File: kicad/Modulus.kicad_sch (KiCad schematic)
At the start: 230 parts, among them J1 XLR3, J2 USB_C_Receptacle_USB2.0_16P, J3 USB_A, J4 USB_A, J5 XLR3, J6 OLED_128x32, P1 Keyswitch, Q1 Keyswitch, SW1 Push_Button, T1 Keyswitch, U1 RP2040, U3 W25Q128JVS, U4 NCP1117-3.3_SOT223, Y1 12MHz, Y2 12MHz

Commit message: added numpad+macropad
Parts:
- added A1: Raspberry_Pi_Pico_THT, PCM_SL_Development_Boards:raspberry_pi_pico_THT, symbol PCM_SL_Development_Board:Raspberry_Pi_Pico_THT
- added D1, D10, D11, D12, D13, D14, D15, D16, D17, D18, D19, D2, D20, D21, D22, D23, D25, D3, D4, D5, D6, D7, D8, D9: Diode, Diode_SMD:D_SMA, symbol SCOTOKEEBS:Placeholder_Diode
- added D24: D_Generic, symbol PCM_4ms_Diode:D_Generic
- added J10, J9: XLR3, NC3FAAH:NEUTRIK_NC3FAAH, symbol Connector_Audio:XLR3
- added S1, S10, S11, S12, S13, S14, S15, S16, S17, S18, S19, S2, S20, S21, S22, S23, S25, S3, S4, S5, S6, S7, S8, S9: ~, symbol ScottoKeebs_KiCAD:Placeholder_Keyswitch
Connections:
- net GND: now also A1.13 (GND), A1.18 (GND), A1.23 (GND), A1.28 (GND), A1.3 (GND), A1.33 (GND), A1.38 (GND), A1.8 (GND), J9.1
- new net: D16.2 (A), S14.2
- new net: D20.2 (A), S19.2
- new net: D4.2 (A), S11.2
- new net: D9.2 (A), S5.2
- new net: D8.2 (A), S4.2
- new net: D14.2 (A), S12.2
- new net: D10.2 (A), S7.2
- new net: D25.2 (A), S25.2
- new net: D17.2 (A), S15.2
- new net: D21.2 (A), S20.2
- new net: D13.2 (A), S10.2
- new net: D2.2 (A), S1.2
- new net: D1.2 (A), S2.2
- new net: D12.2 (A), S9.2
- new net: D11.2 (A), S8.2
- new net: D22.2 (A), S22.2
- new net: D3.2 (A), S6.2
- new net: D6.2 (A), S21.2
- new net: D18.2 (A), S17.2
- new net: D7.2 (A), S3.2
- new net: D15.2 (A), S13.2
- new net: D5.2 (A), S16.2
- new net: D23.2 (A), S23.2
- new net: D19.2 (A), S18.2
- new net NUMPAD_COL_0: A1.21 (GP16), D2.1 (K), D3.1 (K), D4.1 (K), D5.1 (K), D6.1 (K)
- new net NUMPAD_COL_1: A1.22 (GP17), D1.1 (K), D10.1 (K), D7.1 (K), D8.1 (K), D9.1 (K)
- new net NUMPAD_COL_2: A1.24 (GP18), D11.1 (K), D12.1 (K), D13.1 (K), D14.1 (K), D15.1 (K)
- new net NUMPAD_COL_3: A1.25 (GP19), D16.1 (K), D17.1 (K), D18.1 (K), D19.1 (K), D20.1 (K)
- new net NUMPAD_COL_4: A1.26 (GP20), D21.1 (K), D22.1 (K), D23.1 (K), D25.1 (K)
- new net NUMPAD_ROW_0: A1.11 (GP8), S1.1, S14.1, S2.1, S20.1, S8.1
- new net NUMPAD_ROW_1: A1.12 (GP9), S15.1, S22.1, S3.1, S6.1, S9.1
- new net NUMPAD_ROW_2: A1.14 (GP10), S10.1, S11.1, S17.1, S23.1, S4.1
- new net NUMPAD_ROW_3: A1.15 (GP11), S12.1, S16.1, S18.1, S5.1
- new net NUMPAD_ROW_4: A1.16 (GP12), S13.1, S19.1, S21.1, S25.1, S7.1
- new net NUMPAD_XLR_CSn: A1.2 (GP1), J10.1
- new net NUMPAD_XLR_RX: A1.1 (GP0), J10.3
- new net NUMPAD_XLR_SCK: A1.4 (GP2), J9.2
- new net NUMPAD_XLR_TX: A1.5 (GP3), J9.3
- new net POWER: A1.39 (VSYS), D24.1 (K)
- new net UNFILTERED-POWER: D24.2 (A), J10.2
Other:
- moved on the sheet: -_1, -_D1, 0)1, 0)D1, 1!1, 1!D1, 2@1, 2@D1, 3#1, 3#D1, 4$1, 4$D1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

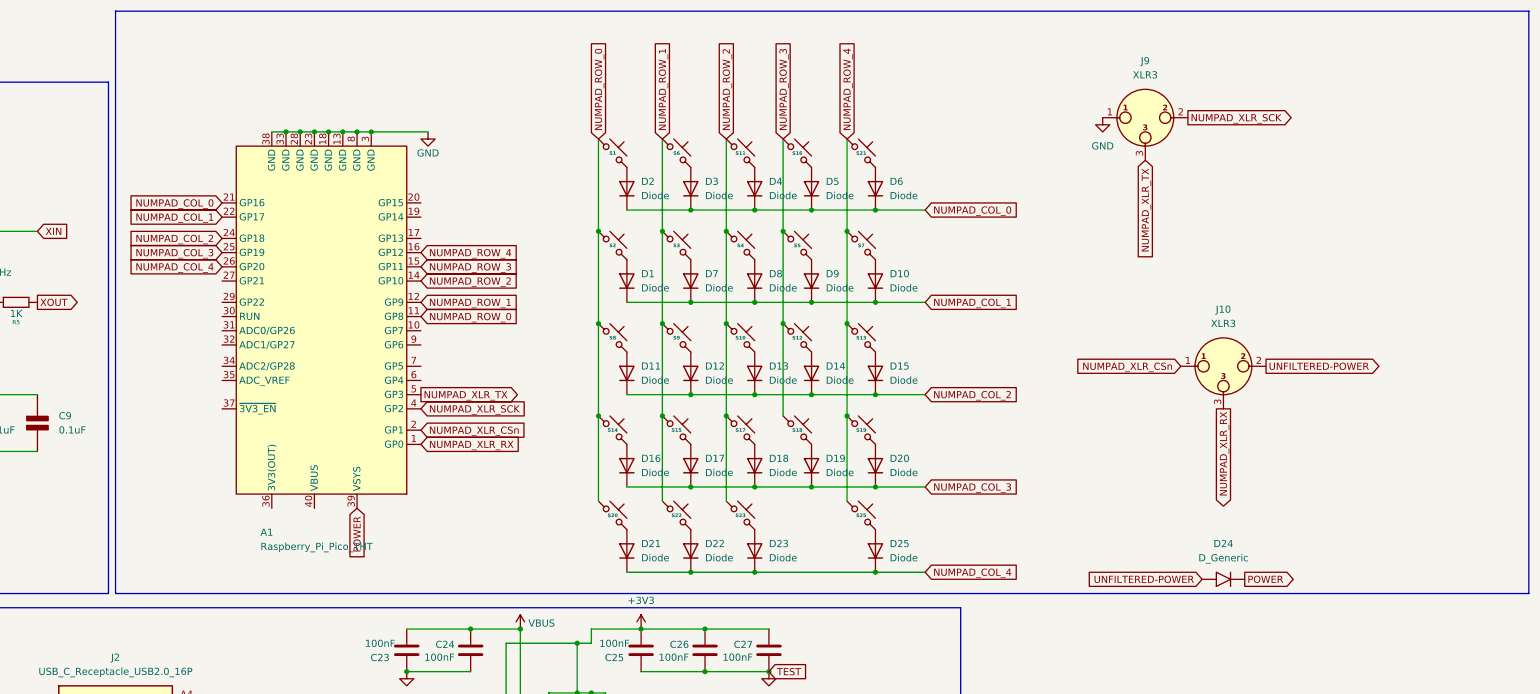
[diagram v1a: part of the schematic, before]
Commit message: removed lock file
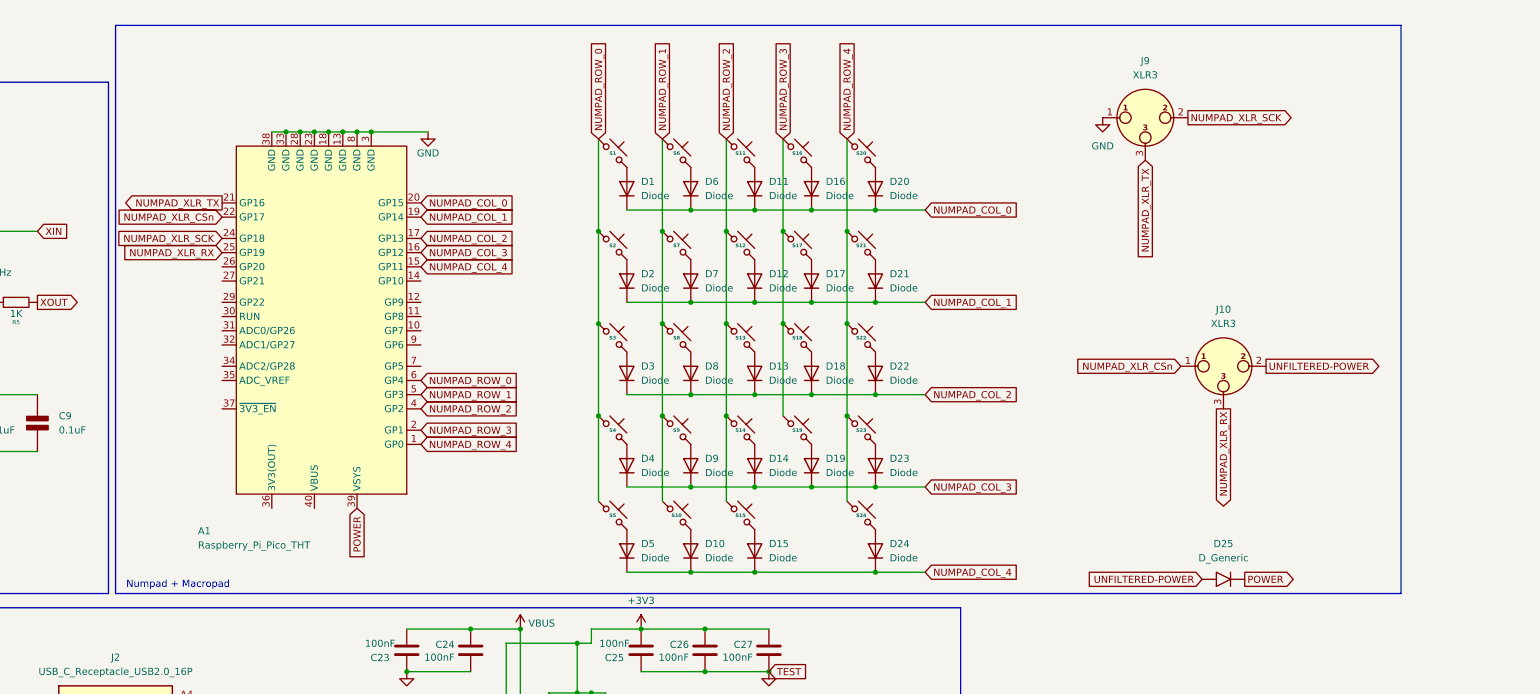
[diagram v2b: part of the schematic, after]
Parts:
- D25: renamed from D24; footprint (none) -> Diode_SMD:D_SMA
- S1, S11, S16, S2, S6: footprint (none) -> PCM_Switch_Keyboard_Hotswap_Kailh:SW_Hotswap_Kailh_MX_1.00u
- S10: renamed from S22; footprint (none) -> PCM_Switch_Keyboard_Hotswap_Kailh:SW_Hotswap_Kailh_MX_1.00u
- S12: renamed from S4; footprint (none) -> PCM_Switch_Keyboard_Hotswap_Kailh:SW_Hotswap_Kailh_MX_1.00u
- S13: renamed from S10; footprint (none) -> PCM_Switch_Keyboard_Hotswap_Kailh:SW_Hotswap_Kailh_MX_1.00u
- S14: renamed from S17; footprint (none) -> PCM_Switch_Keyboard_Hotswap_Kailh:SW_Hotswap_Kailh_MX_1.00u
- S15: renamed from S23; footprint (none) -> PCM_Switch_Keyboard_Hotswap_Kailh:SW_Hotswap_Kailh_MX_1.00u
- S17: renamed from S5; footprint (none) -> PCM_Switch_Keyboard_Hotswap_Kailh:SW_Hotswap_Kailh_MX_1.00u
- S18: renamed from S12; footprint (none) -> PCM_Switch_Keyboard_Hotswap_Kailh:SW_Hotswap_Kailh_MX_1.50u_90deg
- S19: renamed from S18; footprint (none) -> PCM_Switch_Keyboard_Hotswap_Kailh:SW_Hotswap_Kailh_MX_1.50u_90deg
- S20: renamed from S21; footprint (none) -> PCM_Switch_Keyboard_Hotswap_Kailh:SW_Hotswap_Kailh_MX_1.00u
- S21: renamed from S7; footprint (none) -> PCM_Switch_Keyboard_Hotswap_Kailh:SW_Hotswap_Kailh_MX_1.00u
- S22: renamed from S13; footprint (none) -> PCM_Switch_Keyboard_Hotswap_Kailh:SW_Hotswap_Kailh_MX_1.00u
- S23: renamed from S19; footprint (none) -> PCM_Switch_Keyboard_Hotswap_Kailh:SW_Hotswap_Kailh_MX_1.00u
- S24: renamed from S25; footprint (none) -> PCM_Switch_Keyboard_Hotswap_Kailh:SW_Hotswap_Kailh_MX_1.00u
- S3: renamed from S8; footprint (none) -> PCM_Switch_Keyboard_Hotswap_Kailh:SW_Hotswap_Kailh_MX_1.00u
- S4: renamed from S14; footprint (none) -> PCM_Switch_Keyboard_Hotswap_Kailh:SW_Hotswap_Kailh_MX_1.00u
- S5: renamed from S20; footprint (none) -> PCM_Switch_Keyboard_Hotswap_Kailh:SW_Hotswap_Kailh_MX_1.00u
- S7: renamed from S3; footprint (none) -> PCM_Switch_Keyboard_Hotswap_Kailh:SW_Hotswap_Kailh_MX_1.00u
- S8: renamed from S9; footprint (none) -> PCM_Switch_Keyboard_Hotswap_Kailh:SW_Hotswap_Kailh_MX_1.00u
- S9: renamed from S15; footprint (none) -> PCM_Switch_Keyboard_Hotswap_Kailh:SW_Hotswap_Kailh_MX_1.00u
- renumbered D2 to D1, D22 to D10, D4 to D11, D8 to D12, D18 to D14, D23 to D15, D5 to D16, D9 to D17, D14 to D18, D1 to D2, D6 to D20, D10 to D21, D15 to D22, D20 to D23, D25 to D24, D11 to D3, D16 to D4, D21 to D5, D3 to D6, D12 to D8, D17 to D9
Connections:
- net NUMPAD_COL_0: now also A1.20 (GP15); no longer A1.21 (GP16)
- net NUMPAD_COL_1: now also A1.19 (GP14); no longer A1.22 (GP17)
- net NUMPAD_COL_2: now also A1.17 (GP13); no longer A1.24 (GP18)
- net NUMPAD_COL_3: now also A1.16 (GP12); no longer A1.25 (GP19)
- net NUMPAD_COL_4: now also A1.15 (GP11); no longer A1.26 (GP20)
- net NUMPAD_ROW_0: now also A1.6 (GP4); no longer A1.11 (GP8)
- net NUMPAD_ROW_1: now also A1.5 (GP3); no longer A1.12 (GP9)
- net NUMPAD_ROW_2: now also A1.4 (GP2); no longer A1.14 (GP10)
- net NUMPAD_ROW_3: now also A1.2 (GP1); no longer A1.15 (GP11)
- net NUMPAD_ROW_4: now also A1.1 (GP0); no longer A1.16 (GP12)
- net NUMPAD_XLR_CSn: now also A1.22 (GP17); no longer A1.2 (GP1)
- net NUMPAD_XLR_RX: now also A1.25 (GP19); no longer A1.1 (GP0)
- net NUMPAD_XLR_SCK: now also A1.24 (GP18); no longer A1.4 (GP2)
- net NUMPAD_XLR_TX: now also A1.21 (GP16); no longer A1.5 (GP3)
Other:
- note added: "Numpad + Macropad"
